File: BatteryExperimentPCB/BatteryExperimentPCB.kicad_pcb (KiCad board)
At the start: 2 copper layers, 32 parts, among them J1 USB_C_Receptacle_USB2.0_14P, J2 Conn_01x12_Pin, J3 Conn_01x12_Pin, Q1 DMG1012T, SW1 SW_Push, U1 ATtiny3226-M, U2 USBLC6-2P6, U3 BQ25628RYKR

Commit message: more pcb work
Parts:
- moved U3 92.1 mm to (226.9, 78.5), turned to 90 degrees
- moved R4 82.7 mm to (210.0, 70.5)
- moved Q1 77.6 mm to (209.9, 104.5)
- moved R7 77.6 mm to (211.9, 101.0)
- moved R8 77.6 mm to (207.9, 101.0)
- moved R13 72.7 mm to (227.5, 74.8), turned to 90 degrees
- moved R14 69.4 mm to (229.0, 74.8), turned to 90 degrees
- moved R15 62.2 mm to (221.5, 79.0), turned to 180 degrees
- moved C3 53.2 mm to (218.5, 96.0)
- moved C4 53.2 mm to (218.5, 99.0)
- moved C5 53.2 mm to (218.5, 102.0)
- moved C6 53.2 mm to (218.5, 105.0)
- moved D2 53.2 mm to (223.0, 104.1)
- moved L1 53.2 mm to (233.7, 99.0)
- moved R12 51.8 mm to (226.0, 74.8), turned to 90 degrees
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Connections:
- J2 pad 2: PA1 -> Button
- J2 pad 5: Button -> PA1
- J3 pad 2: PC3 -> PA4
- U1 pad 2: PC3 -> Button
- U1 pad 5: Button -> PA4
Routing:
- net Reset: track 0.00 -> 24.5 mm
- net Button: track 0.00 -> 22.9 mm
- net DBUS-: track 4.15 -> 21.4 mm, vias 2 -> 3
- net DBUS+: track 7.66 -> 22.5 mm, vias 0 -> 2
- net Net-(U1-PA5): track 0.00 -> 11.7 mm
- net Battery+: track 0.00 -> 11.0 mm
- net StatusInterrupt: track 0.00 -> 10.2 mm, vias 0 -> 2
- net SDA: track 0.00 -> 7.33 mm, vias 0 -> 2
- net VBUS: track 11.1 -> 18.3 mm
- net SCL: track 0.00 -> 6.70 mm
- net +3.75V: track 0.00 -> 4.53 mm
- net CaseBlue: track 7.92 -> 4.01 mm
- net BulbLED: track 0.00 -> 3.02 mm
- net CaseRed: track 0.00 -> 2.31 mm
- net Net-(D1-RK): track 0.00 -> 2.10 mm
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
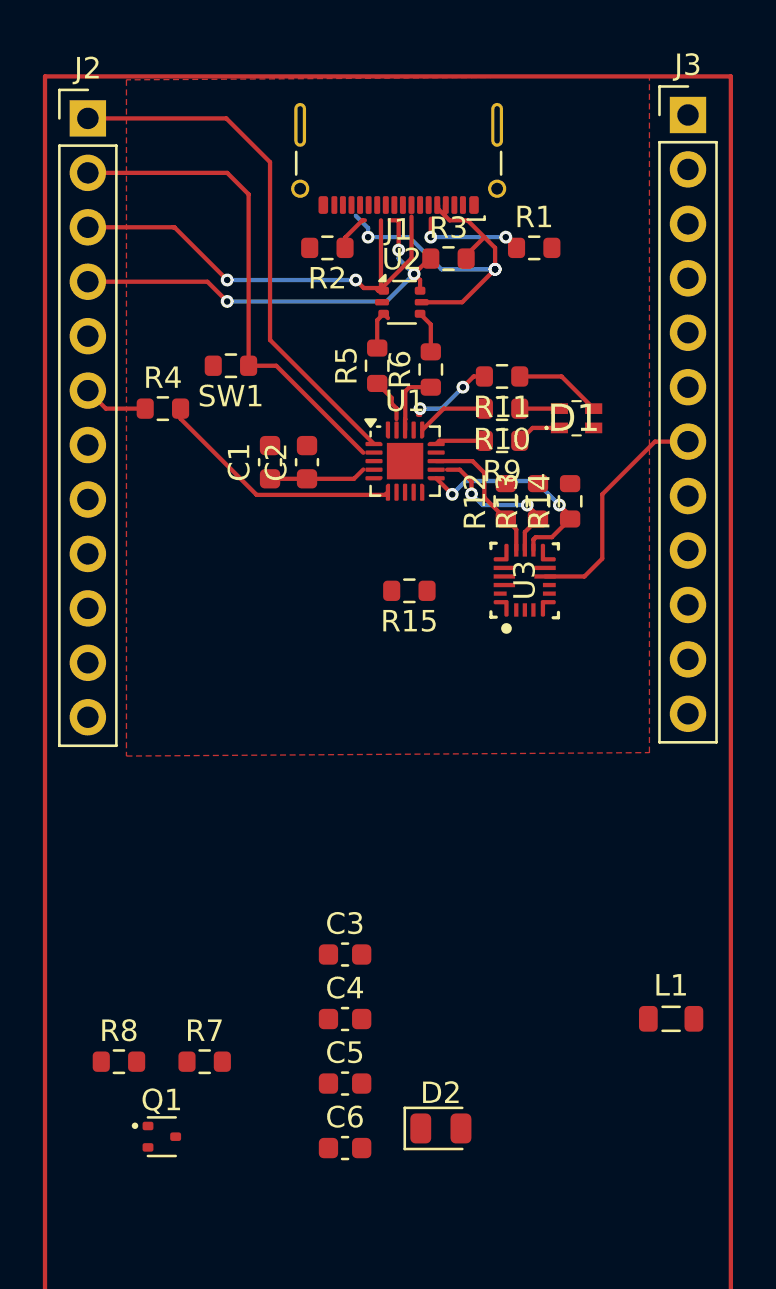
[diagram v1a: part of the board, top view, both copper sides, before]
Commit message: pcb layout attempt with components on top and bottom of a two layer pcb, no ground connections yet
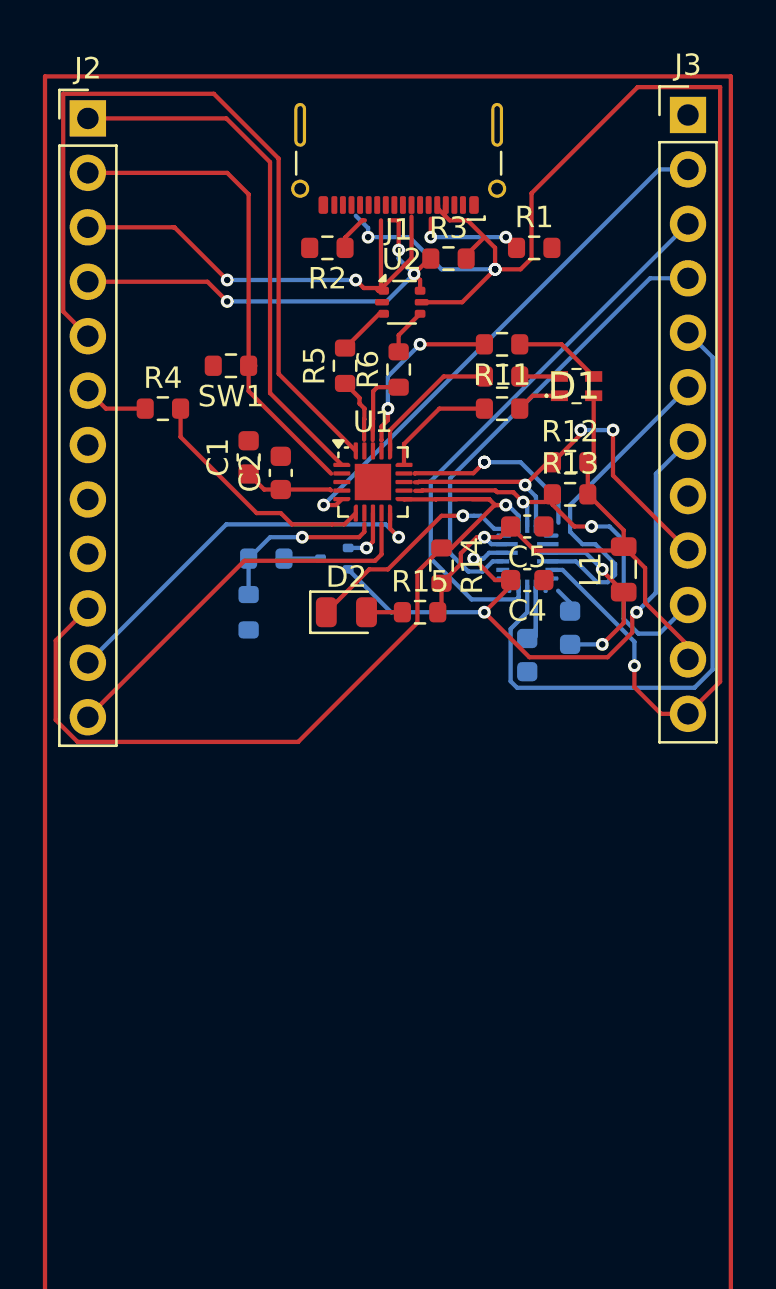
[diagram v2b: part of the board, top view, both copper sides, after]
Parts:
- C3, C6, Q1, R7, R8, U3: moved to B.Cu
- moved Q1 28.1 mm to (218.0, 77.5), turned to 180 degrees
- moved C5 27.3 mm to (227.0, 76.0), turned to 180 degrees
- moved C6 26.4 mm to (229.0, 80.7), turned to -90 degrees
- moved D2 24.5 mm to (218.6, 80.0)
- moved R8 24.5 mm to (214.8, 77.5), turned to 180 degrees
- moved C4 22.2 mm to (227.0, 78.5), turned to 180 degrees
- moved L1 21.1 mm to (231.5, 78.0), turned to 90 degrees
- moved R7 21.1 mm to (214.0, 80.0), turned to 90 degrees
- moved C3 16.4 mm to (227.0, 82.0), turned to 90 degrees
- moved R14 6.71 mm to (223.0, 77.8), turned to -90 degrees
- moved R12 3.51 mm to (229.0, 73.0), turned to 0 degrees
- moved U1 1.79 mm to (219.8, 73.9)
- moved R13 1.53 mm to (229.0, 74.5), turned to 0 degrees
- moved D1 1.50 mm to (229.3, 69.5)
- moved R10 1.50 mm to (225.8, 69.0)
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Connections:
- J2 pad 8: SCL -> GND
- J2 pad 9: SDA -> GND
- J3 pad 10: GND -> SDA
- J3 pad 11: VBUS -> +3.75V
- J3 pad 12: GND -> VBUS
- J3 pad 3: QON -> ILIM
- J3 pad 4: ILIM -> QON
- J3 pad 5: PMID -> PMID_GO
- J3 pad 6: PMID_GO -> PMID
- J3 pad 9: +3.75V -> SCL
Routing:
- net VBUS: track 18.3 -> 74.3 mm, vias 3 -> 4
- net PA1: track 0.00 -> 38.2 mm
- net PMID_GO: track 0.00 -> 30.9 mm
- net StatusInterrupt: track 10.2 -> 40.4 mm, vias 2 -> 1
- net +3.75V: track 4.53 -> 31.7 mm, vias 0 -> 1
- net ILIM: track 0.00 -> 26.0 mm
- net PA4: track 0.00 -> 24.5 mm, vias 0 -> 1
- net QON: track 0.00 -> 21.5 mm
- net Battery+: track 11.0 -> 31.2 mm, vias 0 -> 3
- net PB4: track 0.00 -> 18.7 mm, vias 0 -> 1
- net PB5: track 0.00 -> 18.3 mm
- net PMID: track 0.00 -> 15.9 mm
- net SCL: track 6.70 -> 20.0 mm, vias 0 -> 3
- net SDA: track 7.33 -> 20.0 mm
- net StatusLED: track 0.00 -> 10.4 mm, vias 0 -> 1
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- removed copper zone on F.Cu, net GND

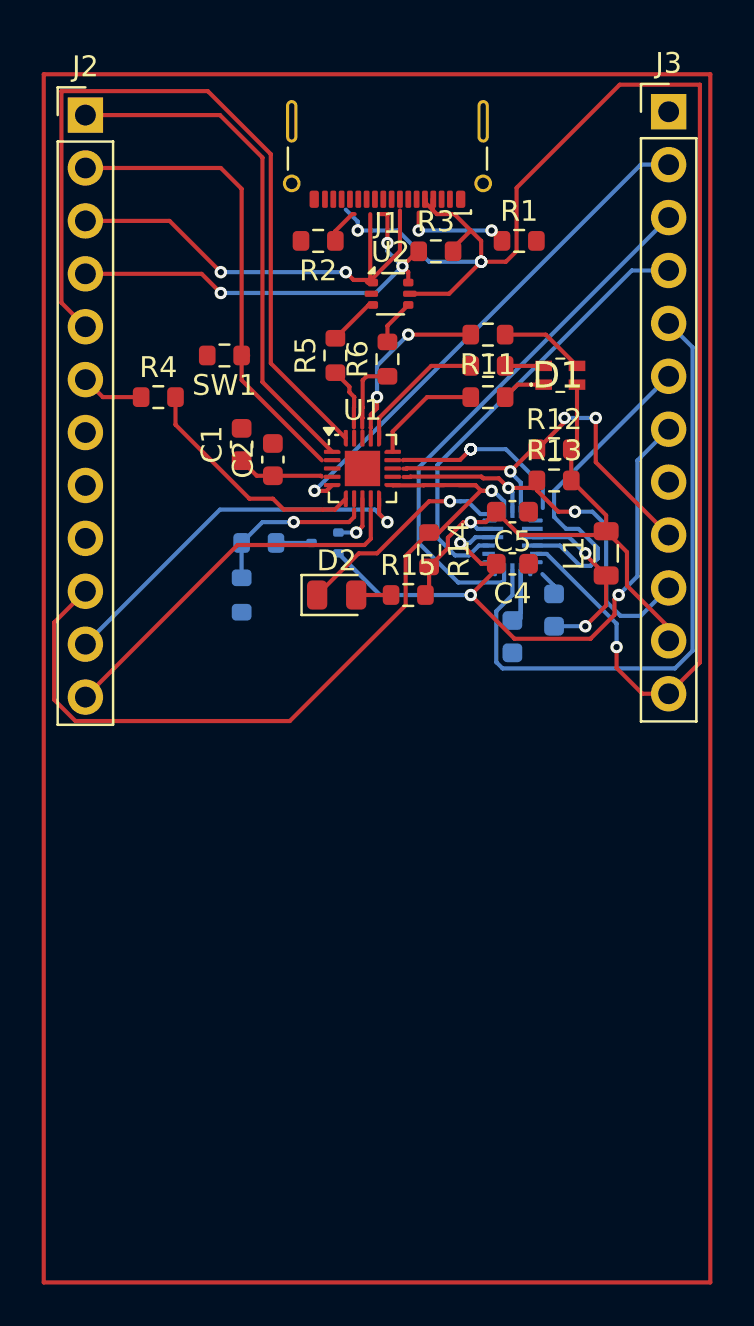
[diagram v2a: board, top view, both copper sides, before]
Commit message: second attempt at pcb design, smaller, using ground zones now
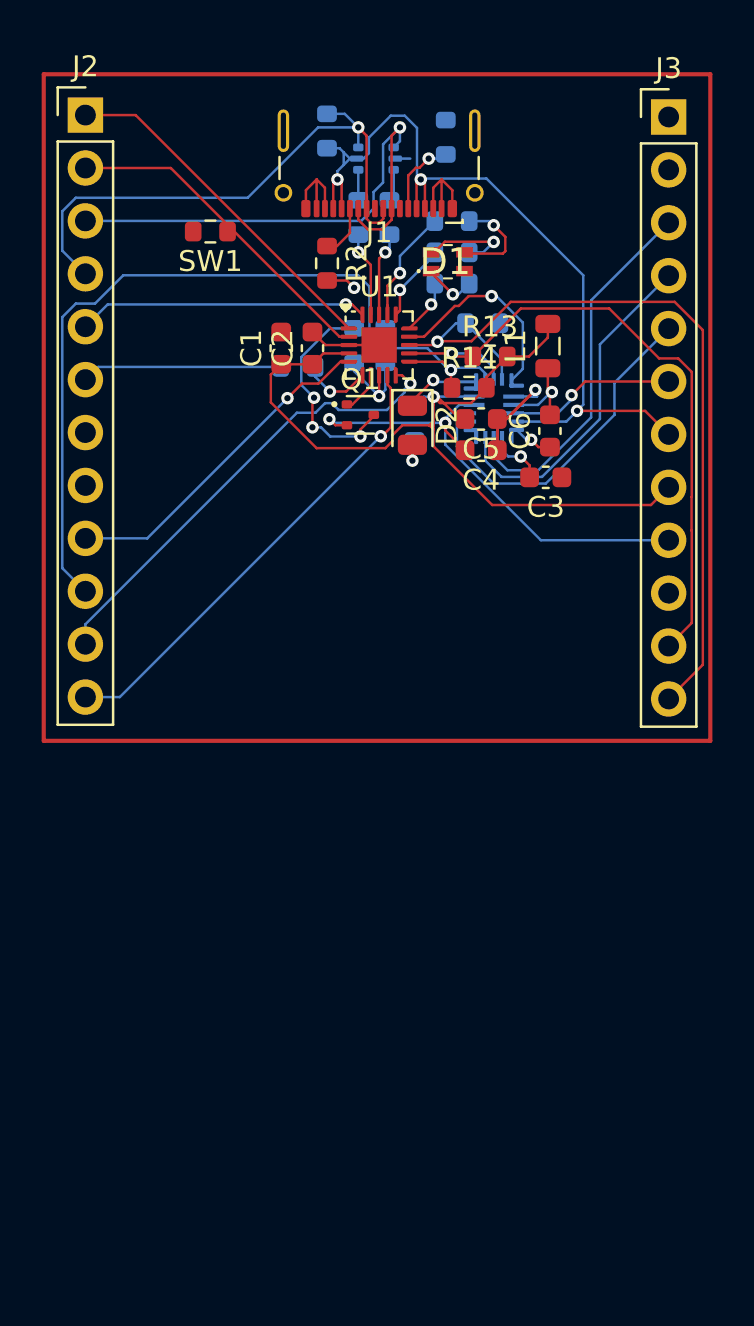
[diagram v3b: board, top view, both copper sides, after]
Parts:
- C3, C6, Q1: moved to F.Cu
- R1, R10, R11, R12, R15, R3, R4, R5, R6, R9, U2: moved to B.Cu
- moved R7 13.8 mm to (220.9, 68.0), turned to -90 degrees
- moved R8 10.5 mm to (219.4, 68.0), turned to -90 degrees
- moved L1 10.3 mm to (228.7, 68.0)
- moved D2 8.92 mm to (222.2, 71.8), turned to -90 degrees
- moved C6 8.60 mm to (228.8, 72.1), turned to 90 degrees
- moved R15 8.26 mm to (222.3, 71.8), turned to 90 degrees
- moved R14 8.01 mm to (224.9, 70.0), turned to 0 degrees
- moved C3 7.82 mm to (228.6, 74.3), turned to 180 degrees
- moved R3 7.79 mm to (218.1, 57.7), turned to -90 degrees
- moved D1 7.67 mm to (223.9, 64.0)
- moved R5 7.12 mm to (221.1, 61.9)
- moved R12 6.95 mm to (225.6, 67.0)
- moved R6 6.94 mm to (219.6, 61.9)
- moved R4 6.86 mm to (216.7, 69.0)
- moved R13 6.70 mm to (225.9, 68.5)
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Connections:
- J2 pad 9: GND -> PA4
- J3 pad 10: SDA -> GND
- J3 pad 11: +3.75V -> SDA
- J3 pad 12: VBUS -> SCL
- J3 pad 2: PA4 -> GND
- J3 pad 3: ILIM -> PMID_GO
- J3 pad 4: QON -> ILIM
- J3 pad 5: PMID_GO -> QON
- J3 pad 7: Battery+ -> VBUS
- J3 pad 8: GND -> +3.75V
- J3 pad 9: SCL -> Battery+
- U1 pad 18: D- -> D+
- U1 pad 19: D+ -> D-
- U1 pad 7: VoltageMonitor -> VoltageMonitorEnable
- U1 pad 8: VoltageMonitorEnable -> VoltageMonitor
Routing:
- net VBUS: track 74.3 -> 40.7 mm, vias 4 -> 3
- net PA1: track 38.2 -> 14.0 mm, vias 0 -> 1
- net GND: track 0.00 -> 24.0 mm, vias 0 -> 2
- net SCL: track 20.0 -> 39.0 mm, vias 3 -> 1
- net PMID_GO: track 30.9 -> 17.8 mm
- net +3.75V: track 31.7 -> 44.0 mm
- net SDA: track 20.0 -> 32.3 mm, vias 2 -> 1
- net ILIM: track 26.0 -> 16.3 mm
- net Net-(Q1-D): track 1.70 -> 10.6 mm, vias 0 -> 3
- net PA4: track 24.5 -> 16.2 mm
- net Net-(U1-PA5): track 11.4 -> 3.36 mm, vias 0 -> 1
- net Reset: track 24.9 -> 16.9 mm
- net PMID: track 15.9 -> 8.20 mm, vias 0 -> 1
- net Battery+: track 31.2 -> 23.8 mm, vias 3 -> 2
- net Button: track 22.9 -> 16.0 mm
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- added copper zone on B.Cu, net GND
- added copper zone on F.Cu, net GND

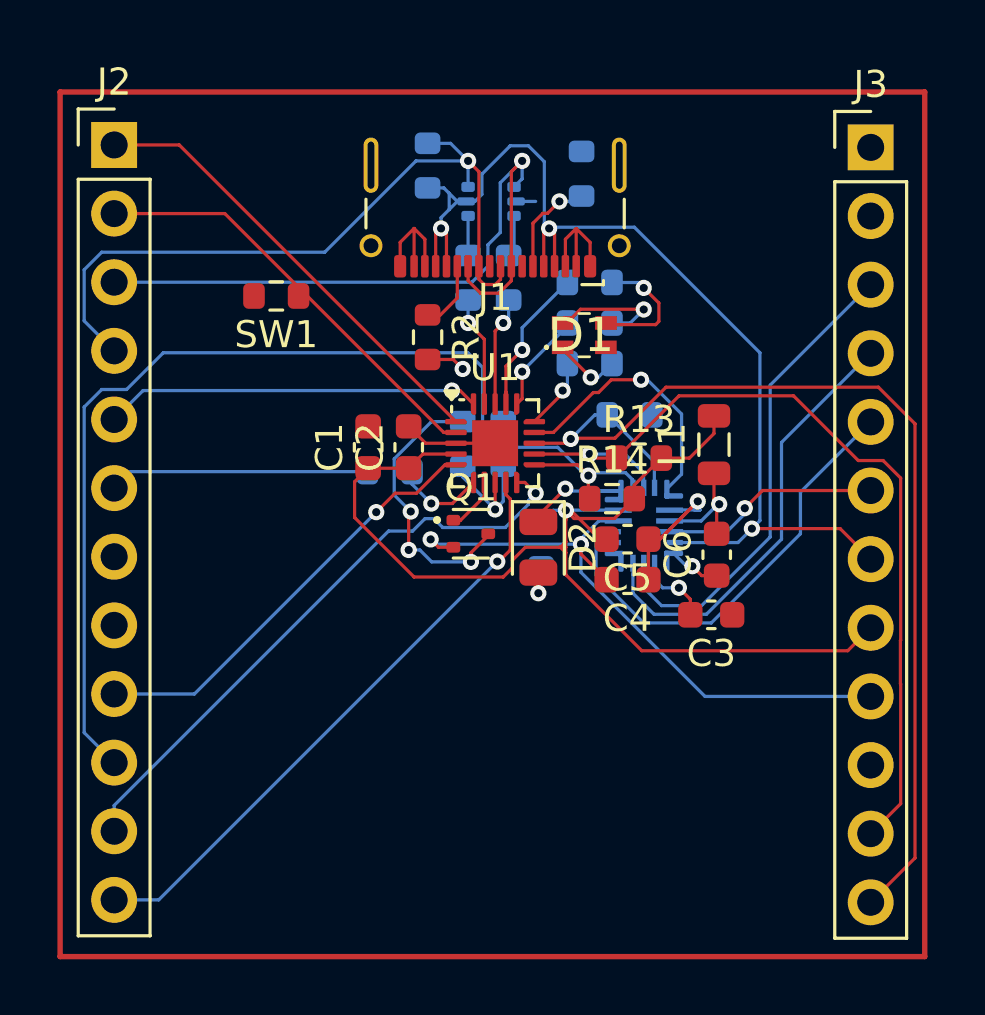
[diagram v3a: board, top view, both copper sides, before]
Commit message: cleaning up connections and fixing errors in rule checker
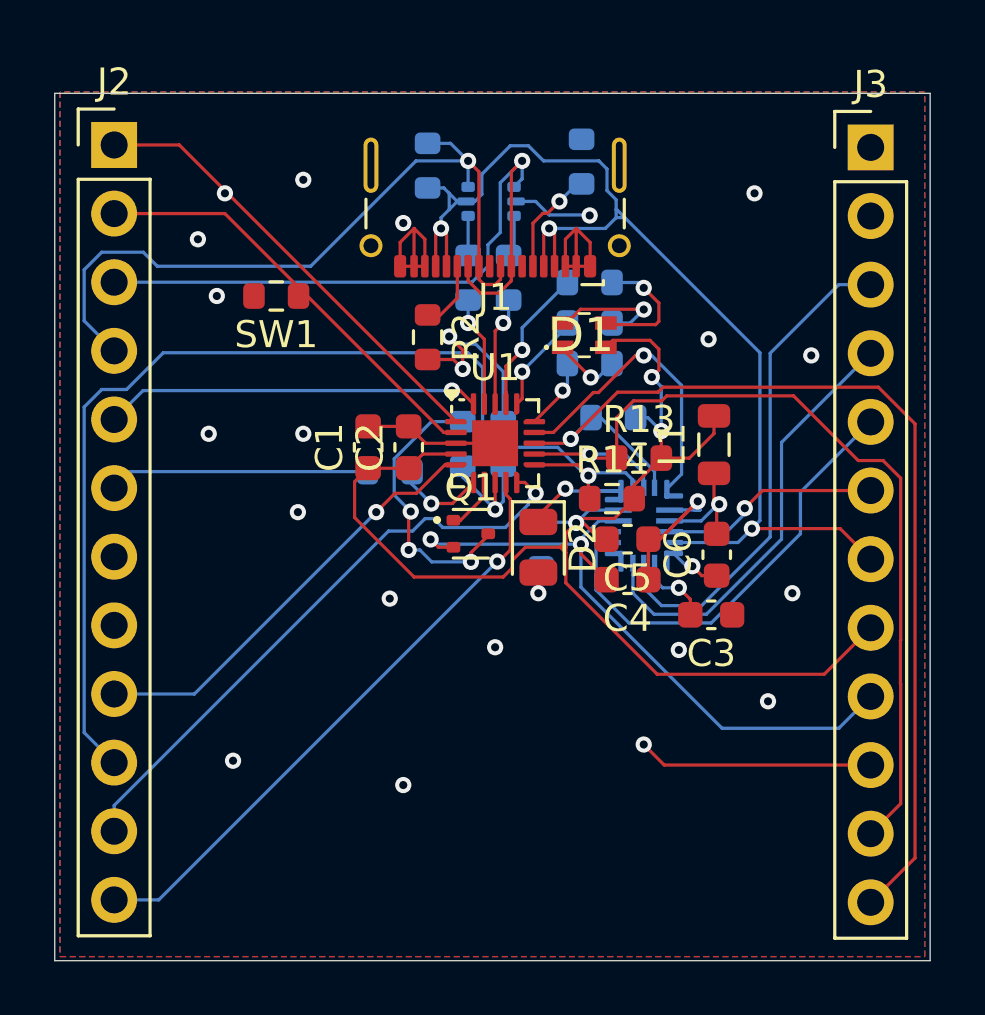
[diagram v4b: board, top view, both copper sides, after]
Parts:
- moved R12 0.61 mm to (225.0, 67.0)
- moved R1 0.45 mm to (223.8, 57.6)
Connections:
- J1 pad GND: (no net) -> GND
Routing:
- net GND: track 24.0 -> 44.1 mm, vias 2 -> 22
- net +3.75V: track 44.0 -> 51.1 mm, vias 1 -> 3
- net VBUS: track 40.7 -> 43.4 mm
- net ChargeEnable: track 9.79 -> 11.2 mm
- net Battery+: track 23.8 -> 25.1 mm
- net SCL: track 39.0 -> 40.0 mm
- net SDA: track 32.3 -> 33.2 mm
- net PMID_GO: track 17.8 -> 18.5 mm
- net Reset: track 16.9 -> 17.0 mm, vias 0 -> 1
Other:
- board outline added: 32.4 x 32.1 mm

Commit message: fixing warning
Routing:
- net StatusLED: track 5.17 -> 3.74 mm
- net GND: track 44.1 -> 45.2 mm, vias 22 -> 21
- net Reset: track 17.0 -> 16.9 mm, vias 1 -> 0
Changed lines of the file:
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@@
+	)
+	(segment
+		(start 218.05 64.9)
+		(end 216.85 63.7)
+		(width 0.12)
+		(layer "F.Cu")
+		(net 1)
 	)
 	(segment
@@
 	)
 	(segment
-		(start 218.1 64.9)
-		(end 219.05 64.9)
-		(width 0.12)
-		(layer "F.Cu")
-		(net 1)
-	)
-	(segment
 		(start 226.86 79.91)
 		(end 226.1 79.15)
@@
 	)
 	(segment
-		(start 218.9 64.05)
-		(end 219.4 64.55)
-		(width 0.12)
-		(layer "F.Cu")
-		(net 1)
-	)
-	(segment
 		(start 224.115 60.565)
 		(end 223.6 60.05)
@@
 	)
 	(segment
-		(start 219.05 64.9)
-		(end 219.4 65.25)
-		(width 0.12)
-		(layer "F.Cu")
-		(net 1)
-	)
-	(segment
-		(start 219.4 64.55)
-		(end 219.4 65.25)
-		(width 0.12)
-		(layer "F.Cu")
-		(net 1)
-	)
-	(segment
 		(start 218.025 68)
 		(end 217.4 67.375)
@@
 	)
 	(segment
+		(start 218.1 64.9)
+		(end 218.05 64.9)
+		(width 0.12)
+		(layer "F.Cu")
+		(net 1)
+	)
+	(segment
 		(start 218 60.45)
 		(end 217.6 60.05)
@@
 	)
 	(via
-		(at 219.4 65.25)
-		(size 0.6)
-		(drill 0.3)
-		(layers "F.Cu" "B.Cu")
-		(net 1)
-	)
-	(via
 		(at 226.1 79.15)
 		(size 0.6)
@@
 	)
 	(via
-		(at 218.9 64.05)
+		(at 216.85 63.7)
 		(size 0.6)
 		(drill 0.3)
@@
 	)
 	(segment
+		(start 216.85 63.7)
+		(end 217.48 64.33)
+		(width 0.12)
+		(layer "B.Cu")
+		(net 1)
+	)
+	(segment
+		(start 228.182 70.468)
+		(end 227.971575 70.468)
+		(width 0.12)
+		(layer "B.Cu")
+		(net 1)
+	)
+	(segment
+		(start 224.08 59.55)
+		(end 222.6 59.55)
+		(width 0.12)
+		(layer "B.Cu")
+		(net 1)
+	)
+	(segment
+		(start 228.1 70.386)
+		(end 228.182 70.468)
+		(width 0.12)
+		(layer "B.Cu")
+		(net 1)
+	)
+	(segment
+		(start 222.6 59.55)
+		(end 222.1 59.05)
+		(width 0.12)
+		(layer "B.Cu")
+		(net 1)
+	)
+	(segment
+		(start 217.48 64.33)
+		(end 219.88 64.33)
+		(width 0.12)
+		(layer "B.Cu")
+		(net 1)
+	)
+	(segment
+		(start 228.1 70.15)
+		(end 228.1 70.386)
+		(width 0.12)
+		(layer "B.Cu")
+		(net 1)
+	)
+	(segment
+		(start 219.88 64.33)
+		(end 220.9 65.35)
+		(width 0.12)
+		(layer "B.Cu")
+		(net 1)
+	)
+	(segment
+		(start 222.1 59.05)
+		(end 221.375 59.05)
+		(width 0.12)
+		(layer "B.Cu")
+		(net 1)
+	)
+	(segment
 		(start 220.9 65.35)
 		(end 220.9 67.2)
@@
 	)
 	(segment
-		(start 228.182 70.468)
-		(end 227.971575 70.468)
-		(width 0.12)
-		(layer "B.Cu")
-		(net 1)
-	)
-	(segment
-		(start 219.88 64.33)
-		(end 220.9 65.35)
-		(width 0.12)
-		(layer "B.Cu")
-		(net 1)
-	)
-	(segment
-		(start 224.08 59.55)
-		(end 222.6 59.55)
-		(width 0.12)
-		(layer "B.Cu")
-		(net 1)
-	)
-	(segment
-		(start 228.1 70.386)
-		(end 228.182 70.468)
-		(width 0.12)
-		(layer "B.Cu")
-		(net 1)
-	)
-	(segment
-		(start 222.6 59.55)
-		(end 222.1 59.05)
-		(width 0.12)
-		(layer "B.Cu")
-		(net 1)
-	)
-	(segment
-		(start 219.18 64.33)
-		(end 219.88 64.33)
-		(width 0.12)
-		(layer "B.Cu")
-		(net 1)
-	)
-	(segment
-		(start 218.9 64.05)
-		(end 219.18 64.33)
-		(width 0.12)
-		(layer "B.Cu")
-		(net 1)
-	)
-	(segment
-		(start 228.1 70.15)
-		(end 228.1 70.386)
-		(width 0.12)
-		(layer "B.Cu")
-		(net 1)
-	)
-	(segment
-		(start 222.1 59.05)
-		(end 221.375 59.05)
-		(width 0.12)
-		(layer "B.Cu")
-		(net 1)
-	)
-	(segment
 		(start 224.85 64.45)
 		(end 224.7 64.45)
@@
 		(start 223.197216 69.68194)
 		(end 223.285276 69.77)
-		(width 0.12)
-		(layer "B.Cu")
-		(net 11)
-	)
-	(segment
-		(start 223.829514 69.77)
-		(end 225.257001 69.77)
 		(width 0.12)
 		(layer "B.Cu")
@@
 	)
 	(segment
-		(start 210.6 58.65)
-		(end 208.91 56.96)
-		(width 0.12)
-		(layer "F.Cu")
-		(net 22)
-	)
-	(segment
 		(start 208.91 56.96)
 		(end 206.5 56.96)
@@
 	(segment
 		(start 219.15 67.2)
-		(end 210.7 58.75)
+		(end 208.91 56.96)
 		(width 0.12)
 		(layer "F.Cu")
 		(net 22)
 	)
-	(segment
-		(start 210.7 58.75)
-		(end 210.6 58.75)
-		(width 0.12)
-		(layer "F.Cu")
-		(net 22)
-	)
-	(segment
-		(start 210.6 58.75)
-		(end 210.6 58.65)
-		(width 0.12)
-		(layer "F.Cu")
-		(net 22)
-	)
-	(via
-		(at 210.6 58.75)
-		(size 0.6)
-		(drill 0.3)
-		(layers "F.Cu" "B.Cu")
-		(net 22)
-	)
